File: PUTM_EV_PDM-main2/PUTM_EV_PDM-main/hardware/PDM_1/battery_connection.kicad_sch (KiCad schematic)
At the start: 3 parts

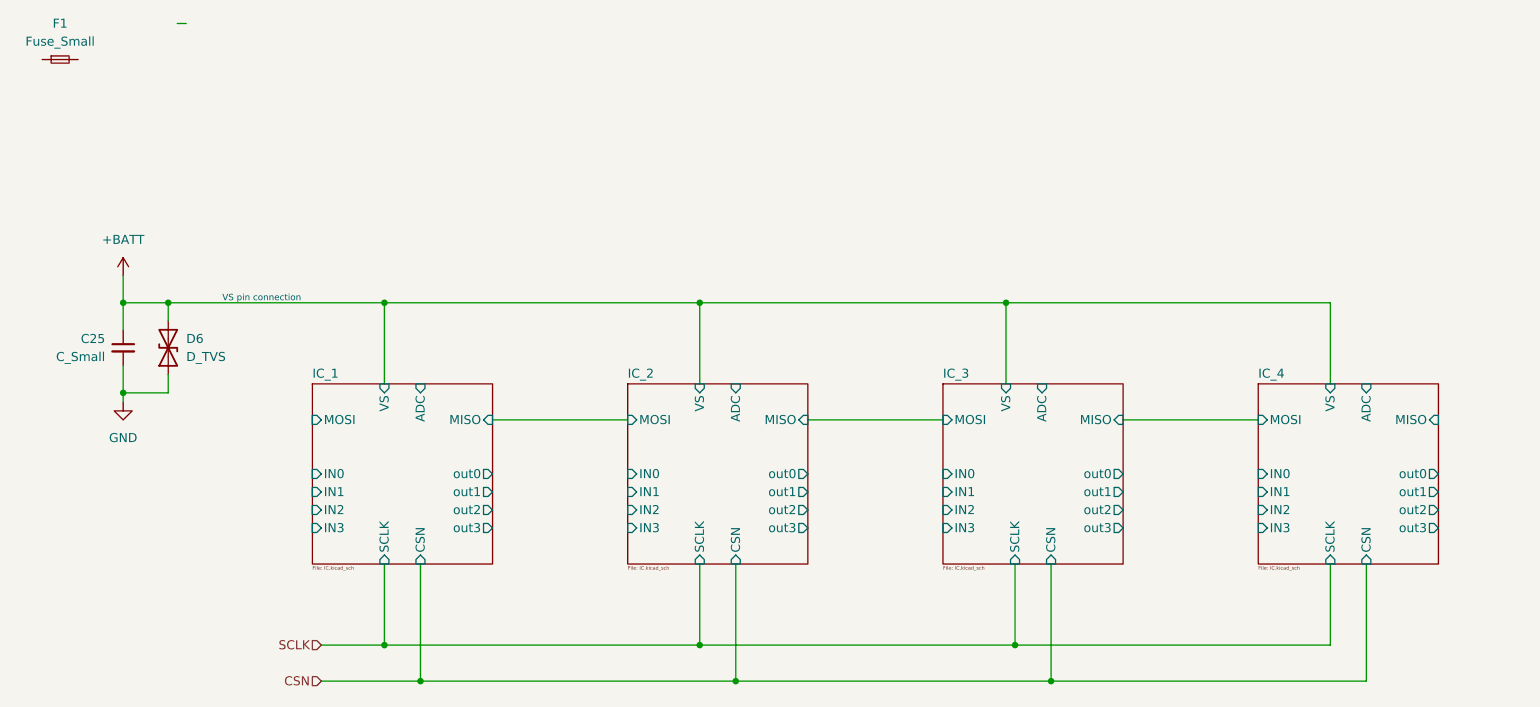
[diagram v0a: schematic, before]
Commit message: nowe połączenia
dodane połączenia z STM
dodane złącza
dodane LED
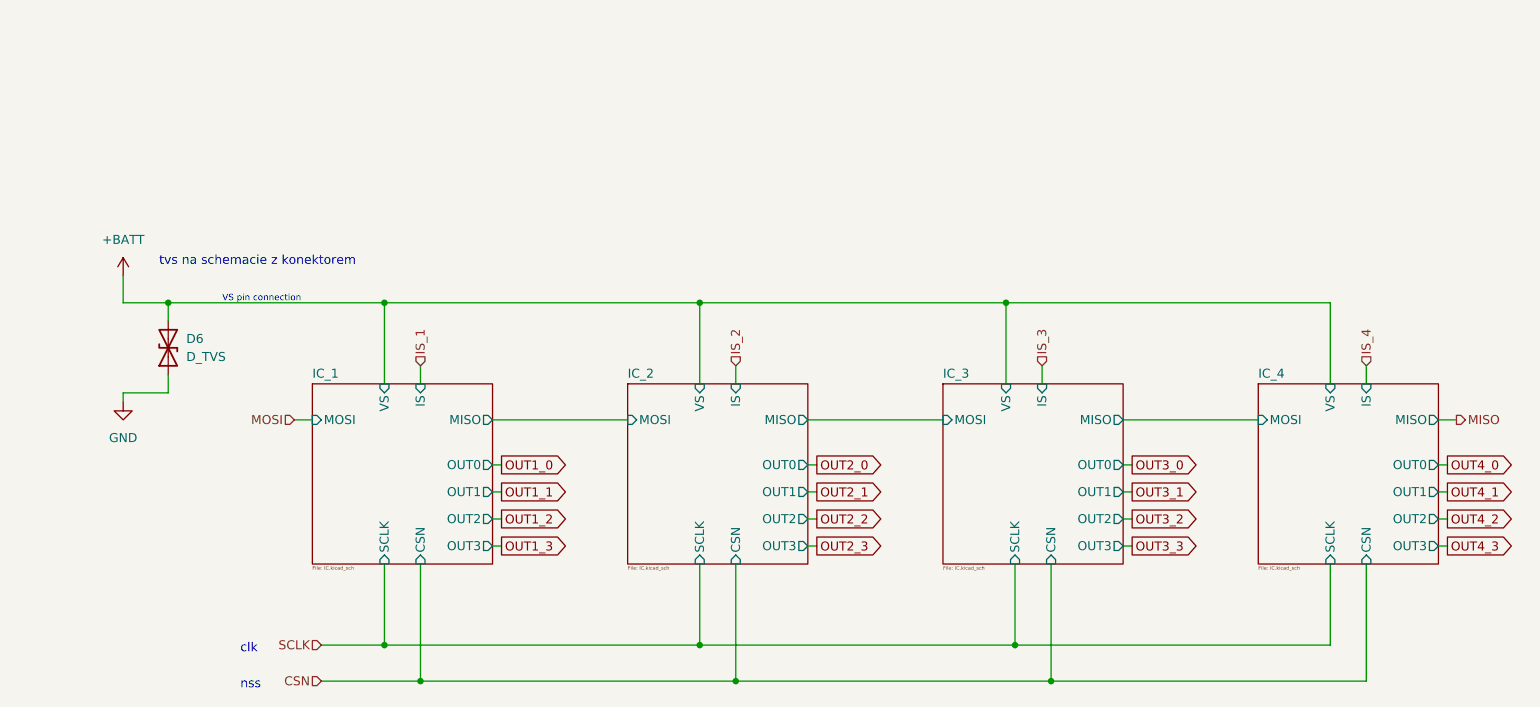
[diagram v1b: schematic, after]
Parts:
- removed C25: C_Small, symbol Device:C_Small
- removed F1: Fuse_Small, symbol Device:Fuse_Small
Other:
- sheet IC_1 ports: added IS, OUT0, OUT1, OUT2, OUT3; removed ADC, IN0, IN1, IN2, IN3, out0, out1, out2, out3
- sheet IC_2 ports: added IS, OUT0, OUT1, OUT2, OUT3; removed ADC, IN0, IN1, IN2, IN3, out0, out1, out2, out3
- sheet IC_3 ports: added IS, OUT0, OUT1, OUT2, OUT3; removed ADC, IN0, IN1, IN2, IN3, out0, out1, out2, out3
- sheet IC_4 ports: added IS, OUT0, OUT1, OUT2, OUT3; removed ADC, IN0, IN1, IN2, IN3, out0, out1, out2, out3
- note added: "clk"
- note added: "nss"
- note added: "tvs na schemacie z konektorem"

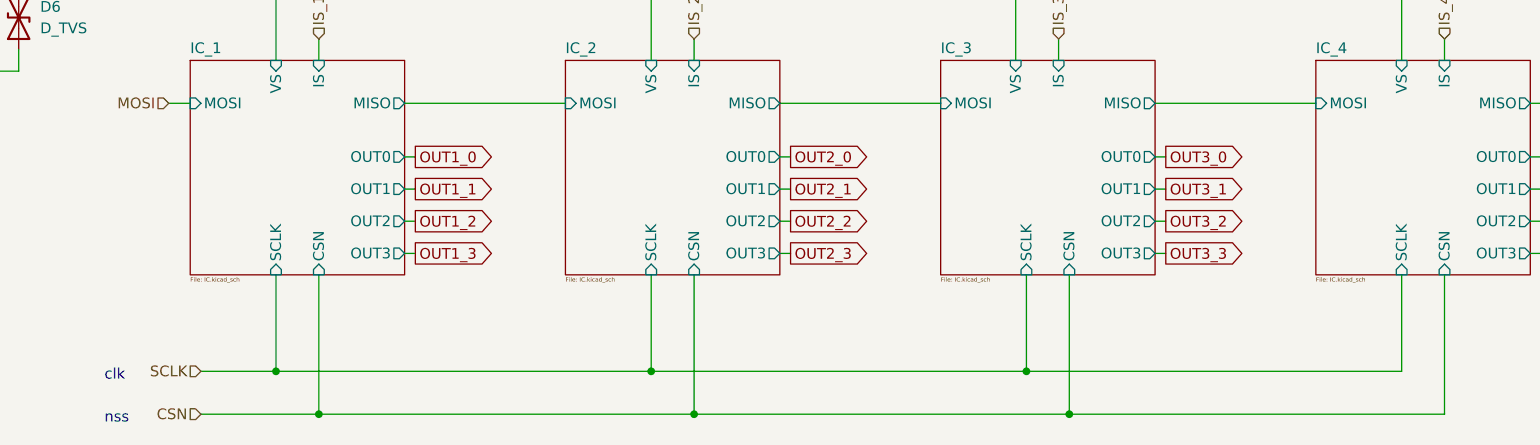
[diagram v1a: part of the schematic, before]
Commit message: małe zmiany
dodano złącza
zmieniono parę footprintów
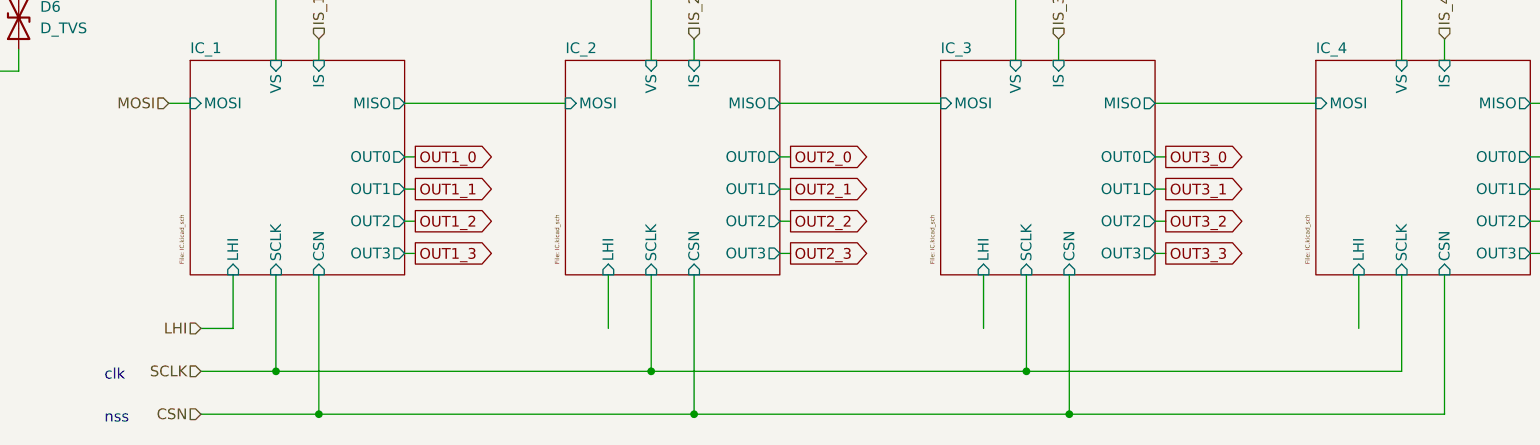
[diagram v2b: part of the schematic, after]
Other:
- sheet IC_1 ports: added LHI; removed none
- sheet IC_2 ports: added LHI; removed none
- sheet IC_3 ports: added LHI; removed none
- sheet IC_4 ports: added LHI; removed none
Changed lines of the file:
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@@
+    (stroke (width 0) (type default))
+  )
+  (wire (pts (xy 64.77 120.65) (xy 68.58 120.65))
     (stroke (width 0) (type default))
   )
@@
     (stroke (width 0) (type default))
   )
+  (wire (pts (xy 68.58 120.65) (xy 68.58 114.3))
+    (stroke (width 0) (type default))
+  )
   (wire (pts (xy 43.18 87.63) (xy 43.18 90.17))
     (stroke (width 0) (type default))
@@
     (stroke (width 0) (type default))
   )
+  (wire (pts (xy 157.48 120.65) (xy 157.48 114.3))
+    (stroke (width 0) (type default))
+  )
   (wire (pts (xy 123.19 114.3) (xy 123.19 130.81))
     (stroke (width 0) (type default))
@@
     (stroke (width 0) (type default))
   )
+  (wire (pts (xy 201.93 120.65) (xy 201.93 114.3))
+    (stroke (width 0) (type default))
+  )
   (wire (pts (xy 177.8 107.95) (xy 179.07 107.95))
     (stroke (width 0) (type default))
@@
   )
   (wire (pts (xy 88.9 111.76) (xy 90.17 111.76))
+    (stroke (width 0) (type default))
+  )
+  (wire (pts (xy 113.03 120.65) (xy 113.03 114.3))
     (stroke (width 0) (type default))
   )
@@
   )
   (hierarchical_label "MOSI" (shape input) (at 60.96 93.98 180) (fields_autoplaced)
+    (effects (font (size 1.27 1.27)) (justify right))
+  )
+  (hierarchical_label "LHI" (shape input) (at 64.77 120.65 180) (fields_autoplaced)
     (effects (font (size 1.27 1.27)) (justify right))
   )
@@
     )
   )
-  (sheet (at 63.5 88.9) (size 25.4 25.4) (fields_autoplaced)
+  (sheet (at 63.5 88.9) (size 25.4 25.4)
     (stroke (width 0.1524) (type solid))
     (fill (color 0 0 0 0.0000))
@@
       (effects (font (size 1.27 1.27)) (justify left bottom))
     )
-    (property "Sheetfile" "IC.kicad_sch" (at 63.5 114.5766 0)
+    (property "Sheetfile" "IC.kicad_sch" (at 62.23 113.03 90)
       (effects (font (size 0.5 0.5)) (justify left top))
     )
@@
     (pin "IS" input (at 78.74 88.9 90)
       (effects (font (size 1.27 1.27)) (justify right))
+    )
+    (pin "LHI" input (at 68.58 114.3 270)
+      (effects (font (size 1.27 1.27)) (justify left))
     )
     (instances
@@
     )
   )
-  (sheet (at 152.4 88.9) (size 25.4 25.4) (fields_autoplaced)
+  (sheet (at 152.4 88.9) (size 25.4 25.4)
     (stroke (width 0.1524) (type solid))
     (fill (color 0 0 0 0.0000))
@@
       (effects (font (size 1.27 1.27)) (justify left bottom))
     )
-    (property "Sheetfile" "IC.kicad_sch" (at 152.4 114.5766 0)
+    (property "Sheetfile" "IC.kicad_sch" (at 151.13 113.03 90)
       (effects (font (size 0.5 0.5)) (justify left top))
     )
@@
     (pin "IS" input (at 166.37 88.9 90)
       (effects (font (size 1.27 1.27)) (justify right))
+    )
+    (pin "LHI" input (at 157.48 114.3 270)
+      (effects (font (size 1.27 1.27)) (justify left))
     )
     (instances
@@
     )
   )
-  (sheet (at 107.95 88.9) (size 25.4 25.4) (fields_autoplaced)
+  (sheet (at 107.95 88.9) (size 25.4 25.4)
     (stroke (width 0.1524) (type solid))
     (fill (color 0 0 0 0.0000))
@@
       (effects (font (size 1.27 1.27)) (justify left bottom))
     )
-    (property "Sheetfile" "IC.kicad_sch" (at 107.95 114.5766 0)
+    (property "Sheetfile" "IC.kicad_sch" (at 106.68 113.03 90)
       (effects (font (size 0.5 0.5)) (justify left top))
     )
@@
     (pin "IS" input (at 123.19 88.9 90)
       (effects (font (size 1.27 1.27)) (justify right))
+    )
+    (pin "LHI" input (at 113.03 114.3 270)
+      (effects (font (size 1.27 1.27)) (justify left))
     )
     (instances
@@
     )
   )
-  (sheet (at 196.85 88.9) (size 25.4 25.4) (fields_autoplaced)
+  (sheet (at 196.85 88.9) (size 25.4 25.4)
     (stroke (width 0.1524) (type solid))
     (fill (color 0 0 0 0.0000))
@@
       (effects (font (size 1.27 1.27)) (justify left bottom))
     )
-    (property "Sheetfile" "IC.kicad_sch" (at 196.85 114.5766 0)
+    (property "Sheetfile" "IC.kicad_sch" (at 195.58 113.03 90)
       (effects (font (size 0.5 0.5)) (justify left top))
     )
@@
       (effects (font (size 1.27 1.27)) (justify right))
     )
-    (instances
+    (pin "LHI" input (at 201.93 114.3 270)
+      (effects (font (size 1.27 1.27)) (justify left))
+    )
+    (instances

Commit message: piny na płytce
Dodano ułożenie pinów na płytce
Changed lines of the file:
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@@
+    (stroke (width 0) (type default))
+  )
+  (wire (pts (xy 199.39 120.65) (xy 201.93 120.65))
     (stroke (width 0) (type default))
   )
@@
     (stroke (width 0) (type default))
   )
+  (wire (pts (xy 110.49 120.65) (xy 113.03 120.65))
+    (stroke (width 0) (type default))
+  )
   (wire (pts (xy 177.8 93.98) (xy 196.85 93.98))
     (stroke (width 0) (type default))
@@
   )
   (wire (pts (xy 88.9 111.76) (xy 90.17 111.76))
+    (stroke (width 0) (type default))
+  )
+  (wire (pts (xy 154.94 120.65) (xy 157.48 120.65))
     (stroke (width 0) (type default))
   )
@@
     (effects (font (size 1.27 1.27)) (justify right))
   )
+  (hierarchical_label "LHI_3" (shape input) (at 154.94 120.65 180) (fields_autoplaced)
+    (effects (font (size 1.27 1.27)) (justify right))
+  )
   (hierarchical_label "MOSI" (shape input) (at 60.96 93.98 180) (fields_autoplaced)
     (effects (font (size 1.27 1.27)) (justify right))
   )
-  (hierarchical_label "LHI" (shape input) (at 64.77 120.65 180) (fields_autoplaced)
+  (hierarchical_label "LHI_4" (shape input) (at 199.39 120.65 180) (fields_autoplaced)
+    (effects (font (size 1.27 1.27)) (justify right))
+  )
+  (hierarchical_label "LHI_1" (shape input) (at 64.77 120.65 180) (fields_autoplaced)
     (effects (font (size 1.27 1.27)) (justify right))
   )
@@
     (effects (font (size 1.27 1.27)) (justify left))
   )
+  (hierarchical_label "LHI_2" (shape input) (at 110.49 120.65 180) (fields_autoplaced)
+    (effects (font (size 1.27 1.27)) (justify right))
+  )
   (hierarchical_label "IS_4" (shape input) (at 212.09 86.36 90) (fields_autoplaced)

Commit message: Koniec połączeń sygnałów
Wszystkie sygnały z stm poprowadzone
Zmienione ułożenie połączeń do złącz
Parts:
- D6: now not fitted
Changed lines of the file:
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@@
+    (effects (font (size 1.27 1.27)) (justify left bottom))
+  )
+  (label "MISO_1" (at 93.98 93.98 0) (fields_autoplaced)
+    (effects (font (size 1.27 1.27)) (justify left bottom))
+  )
+  (label "MISO_2" (at 140.97 93.98 0) (fields_autoplaced)
+    (effects (font (size 1.27 1.27)) (justify left bottom))
+  )
+  (label "MISO_3" (at 184.15 93.98 0) (fields_autoplaced)
     (effects (font (size 1.27 1.27)) (justify left bottom))
   )
@@
   )
   (symbol (lib_id "Device:D_TVS") (at 43.18 83.82 90) (unit 1)
-    (in_bom yes) (on_board yes) (dnp no) (fields_autoplaced)
+    (in_bom yes) (on_board no) (dnp yes) (fields_autoplaced)
     (property "Reference" "D6" (at 45.72 82.55 90)
       (effects (font (size 1.27 1.27)) (justify right))
